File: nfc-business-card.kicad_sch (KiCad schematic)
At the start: 3 parts, among them U1 NT3H2111W0FHKH

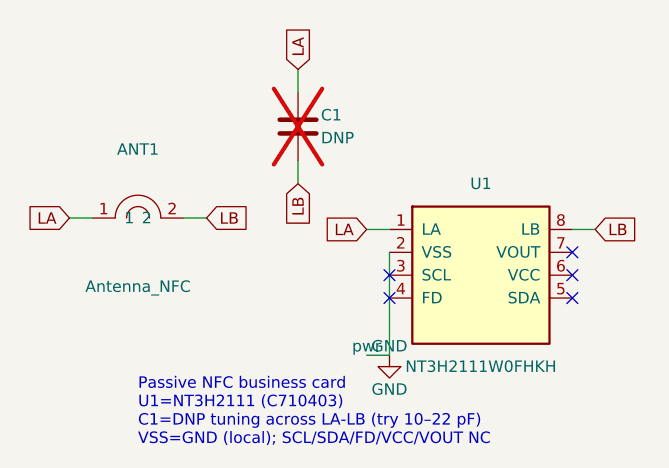
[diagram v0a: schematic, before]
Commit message: feat(stability): NC pull-downs, C1 BOM fix, and tuned assembly exports
Add DNP R2–R6 (100 kΩ to VSS on B.Cu) for floating NC pins, lock C1 to
Walsin 10 pF NP0 (C301961), and export bom-c1/positions-c1 for JLC SMT.
Correct wrong LCSC IDs in parts.md and add tune_antenna.py for C1/turn trim.

Co-authored-by: Cursor <cursoragent@cursor.com>
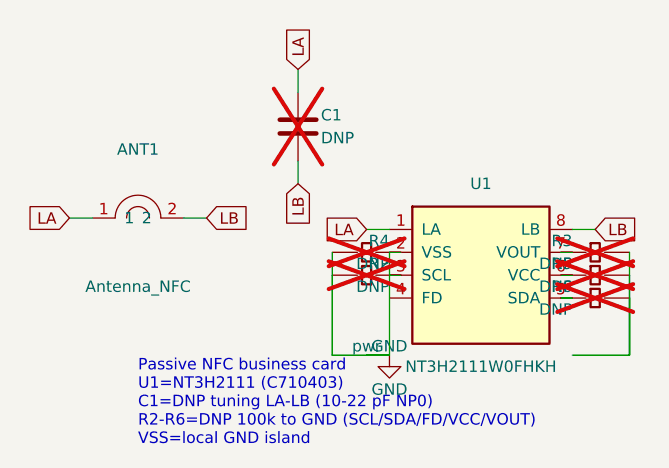
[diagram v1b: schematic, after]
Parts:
- added R2, R3, R4, R5, R6: DNP, NFC_BusinessCard:R_0402_1005Metric, symbol NFC_BusinessCard:R_0402
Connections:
- net GND: now also R2.1, R4.1, R4.2
- net at U1.3 (SCL): now also R2.2
- net at U1.5 (SDA): now also R6.2
- net at U1.6 (VCC): now also R5.2
- net at U1.7 (VOUT): now also R3.2
- new net: R3.1, R5.1, R6.1
- no-connect marks 5 -> 0
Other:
- note added: "Passive NFC business card U1=NT3H2111 (C710403) C1=DNP tuning LA-LB (10-22 pF NP0) R2-R6=DNP 100k to GND (SCL/SDA/FD/VCC/VOUT) VSS=local GND island"
- note removed: "Passive NFC business card U1=NT3H2111 (C710403) C1=DNP tuning across LA-LB (try 10–22 pF) VSS=GND (local); SCL/SDA/FD/VCC/VOUT NC"
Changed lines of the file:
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@@
 	(wire (pts (xy 116.84 82.55) (xy 116.84 93.98)) (stroke (width 0) (type default)))
 	(wire (pts (xy 116.84 93.98) (xy 114.3 93.98)) (stroke (width 0) (type default)))
-	(no_connect (at 116.84 85.09))
-	(no_connect (at 116.84 87.63))
-	(no_connect (at 137.16 82.55))
-	(no_connect (at 137.16 85.09))
-	(no_connect (at 137.16 87.63))
-	(text "Passive NFC business card\nU1=NT3H2111 (C710403)\nC1=DNP tuning across LA-LB (try 10–22 pF)\nVSS=GND (local); SCL/SDA/FD/VCC/VOUT NC"
+	(symbol
+		(lib_id "NFC_BusinessCard:R_0402")
+		(at 114.3 85.09 90)
+		(unit 1)
+		(exclude_from_sim no)
+		(in_bom no)
+		(on_board yes)
+		(dnp yes)
+		(property "Reference" "R2" (at 116.84 83.82000000000001 90) (effects (font (size 1.27 1.27)) (justify left)))
+		(property "Value" "DNP" (at 116.84 86.36 90) (effects (font (size 1.27 1.27)) (justify left)))
+		(property "Footprint" "NFC_BusinessCard:R_0402_1005Metric" (at 114.3 85.09 90) (effects (font (size 1.27 1.27)) (hide yes)))
+		(property "LCSC Part #" "C25744" (at 114.3 85.09 90) (effects (font (size 1.27 1.27)) (hide yes)))
+		(pin "1")
+		(pin "2")
+		(instances (project "nfc-business-card" (path "/db0e1d12-1252-490b-9c29-4e9a9001ab69" (reference "R2") (unit 1))))
+	)
+	(wire (pts (xy 116.84 85.09) (xy 118.11 85.09)) (stroke (width 0) (type default)))
+	(wire (pts (xy 110.49 85.09) (xy 110.49 93.98)) (stroke (width 0) (type default)))
+	(symbol
+		(lib_id "NFC_BusinessCard:R_0402")
+		(at 114.3 82.55 90)
+		(unit 1)
+		(exclude_from_sim no)
+		(in_bom no)
+		(on_board yes)
+		(dnp yes)
+		(property "Reference" "R4" (at 116.84 81.28 90) (effects (font (size 1.27 1.27)) (justify left)))
+		(property "Value" "DNP" (at 116.84 83.82 90) (effects (font (size 1.27 1.27)) (justify left)))
+		(property "Footprint" "NFC_BusinessCard:R_0402_1005Metric" (at 114.3 82.55 90) (effects (font (size 1.27 1.27)) (hide yes)))
+		(property "LCSC Part #" "C25744" (at 114.3 82.55 90) (effects (font (size 1.27 1.27)) (hide yes)))
+		(pin "1")
+		(pin "2")
+		(instances (project "nfc-business-card" (path "/db0e1d12-1252-490b-9c29-4e9a9001ab69" (reference "R4") (unit 1))))
+	)
+	(wire (pts (xy 116.84 82.55) (xy 118.11 82.55)) (stroke (width 0) (type default)))
+	(wire (pts (xy 110.49 82.55) (xy 110.49 93.98)) (stroke (width 0) (type default)))
+	(symbol
+		(lib_id "NFC_BusinessCard:R_0402")
+		(at 139.7 82.55 270)
+		(unit 1)
+		(exclude_from_sim no)
+		(in_bom no)
+		(on_board yes)
+		(dnp yes)
+		(property "Reference" "R3" (at 137.16 81.28 270) (effects (font (size 1.27 1.27)) (justify left)))
+		(property "Value" "DNP" (at 137.16 83.82 270) (effects (font (size 1.27 1.27)) (justify left)))
+		(property "Footprint" "NFC_BusinessCard:R_0402_1005Metric" (at 139.7 82.55 270) (effects (font (size 1.27 1.27)) (hide yes)))
+		(property "LCSC Part #" "C25744" (at 139.7 82.55 270) (effects (font (size 1.27 1.27)) (hide yes)))
+		(pin "1")
+		(pin "2")
+		(instances (project "nfc-business-card" (path "/db0e1d12-1252-490b-9c29-4e9a9001ab69" (reference "R3") (unit 1))))
+	)
+	(wire (pts (xy 137.16 82.55) (xy 135.89 82.55)) (stroke (width 0) (type default)))
+	(wire (pts (xy 143.51 82.55) (xy 143.51 93.98)) (stroke (width 0) (type default)))
+	(symbol
+		(lib_id "NFC_BusinessCard:R_0402")
+		(at 139.7 85.09 270)
+		(unit 1)
+		(exclude_from_sim no)
+		(in_bom no)
+		(on_board yes)
+		(dnp yes)
+		(property "Reference" "R5" (at 137.16 83.82000000000001 270) (effects (font (size 1.27 1.27)) (justify left)))
+		(property "Value" "DNP" (at 137.16 86.36 270) (effects (font (size 1.27 1.27)) (justify left)))
+		(property "Footprint" "NFC_BusinessCard:R_0402_1005Metric" (at 139.7 85.09 270) (effects (font (size 1.27 1.27)) (hide yes)))
+		(property "LCSC Part #" "C25744" (at 139.7 85.09 270) (effects (font (size 1.27 1.27)) (hide yes)))
+		(pin "1")
+		(pin "2")
+		(instances (project "nfc-business-card" (path "/db0e1d12-1252-490b-9c29-4e9a9001ab69" (reference "R5") (unit 1))))
+	)
+	(wire (pts (xy 137.16 85.09) (xy 135.89 85.09)) (stroke (width 0) (type default)))
+	(wire (pts (xy 143.51 85.09) (xy 143.51 93.98)) (stroke (width 0) (type default)))
+	(symbol
+		(lib_id "NFC_BusinessCard:R_0402")
+		(at 139.7 87.63 270)
+		(unit 1)
+		(exclude_from_sim no)
+		(in_bom no)
+		(on_board yes)
+		(dnp yes)
+		(property "Reference" "R6" (at 137.16 86.36 270) (effects (font (size 1.27 1.27)) (justify left)))
+		(property "Value" "DNP" (at 137.16 88.89999999999999 270) (effects (font (size 1.27 1.27)) (justify left)))
+		(property "Footprint" "NFC_BusinessCard:R_0402_1005Metric" (at 139.7 87.63 270) (effects (font (size 1.27 1.27)) (hide yes)))
+		(property "LCSC Part #" "C25744" (at 139.7 87.63 270) (effects (font (size 1.27 1.27)) (hide yes)))
+		(pin "1")
+		(pin "2")
+		(instances (project "nfc-business-card" (path "/db0e1d12-1252-490b-9c29-4e9a9001ab69" (reference "R6") (unit 1))))
+	)
+	(wire (pts (xy 137.16 87.63) (xy 135.89 87.63)) (stroke (width 0) (type default)))
+	(wire (pts (xy 143.51 87.63) (xy 143.51 93.98)) (stroke (width 0) (type default)))
+	(wire (pts (xy 110.49 93.98) (xy 116.84 93.98)) (stroke (width 0) (type default)))
+	(wire (pts (xy 116.84 93.98) (xy 116.84 93.98)) (stroke (width 0) (type default)))
+	(wire (pts (xy 143.51 93.98) (xy 137.16 93.98)) (stroke (width 0) (type default)))
+	(wire (pts (xy 137.16 93.98) (xy 137.16 93.98)) (stroke (width 0) (type default)))
+	(text "Passive NFC business card\nU1=NT3H2111 (C710403)\nC1=DNP tuning LA-LB (10-22 pF NP0)\nR2-R6=DNP 100k to GND (SCL/SDA/FD/VCC/VOUT)\nVSS=local GND island"
 		(at 88.9 104.14 0)
 		(effects (font (size 1.27 1.27)) (justify left bottom))
